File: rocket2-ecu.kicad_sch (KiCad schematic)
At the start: 42 parts, among them J1 ALARM, J12 SMA, J13 ARM Cortex Debug, P1 PAD_SMD, P2 PAD_SMD, P3 PAD_SMD, P4 PAD_SMD, Q1 DMG3402L, U36 AZ1117-3.3

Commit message: Lots of cleanup and updates; Waiting on PR approval for GPS filter
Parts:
- removed C5, C8, C9: 100nF, Capacitor_SMD:C_0603_1608Metric, symbol Device:C_Small
- removed C53, C54, C55: 10uF, Capacitor_SMD:C_0603_1608Metric, symbol Device:C_Small
- removed D35, D36: ESD321, Diode_SMD:D_0402_1005Metric, symbol Device:D_Zener_Small
- removed J13: ARM Cortex Debug, Connector_PinHeader_1.27mm:PinHeader_2x05_P1.27mm_Vertical_SMD, symbol UCIRP-KiCAD-Lib:ARM_Cortex_Debug
- removed J14: ~, Connector_USB:USB_C_Receptacle_GCT_USB4105-xx-A_16P_TopMnt_Horizontal, symbol UCIRP-KiCAD-Lib:USB-C
- removed R3, R4: 4k7, Resistor_SMD:R_0603_1608Metric, symbol Device:R_Small_US
- removed R84, R85: 5.1K, Resistor_SMD:R_0603_1608Metric, symbol Device:R_Small_US
- removed U36: AZ1117-3.3, Package_TO_SOT_SMD:SOT-223-3_TabPin2, symbol Regulator_Linear:AZ1117-3.3
- removed U4: ~, RF_GPS:ublox_SAM-M8Q, symbol UCIRP-KiCAD-Lib:SAM-M8Q
- removed U6: ~, Package_QFP:LQFP-176_24x24mm_P0.5mm, symbol UCIRP-KiCAD-Lib:STM32F469IIT6
- renumbered C6 to C5, C7 to C6, C52 to C7, C51 to C8, J12 to J2, R5 to R3, R6 to R4, U5 to U4, U35 to U5, U34 to U6
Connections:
- no-connect marks 13 -> 0
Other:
- added sheet ECU_STM32 (ecu_stm32.kicad_sch)
- added sheet EVE_GPS (eve_gps.kicad_sch)
- note added: "ETHERNET"
- note added: "STM32 + USB + DEBUG"
- note added: "TRS Radio Module"
- note removed: "*IMPORTANT*"
- note removed: "PCB Considerations (PAGE 12)"
- note removed: "REF (PG 11)"
- company: (none) -> UCI Rocket Project Liquids
- title: (none) -> Rocket2 ECU
- moved on the sheet: C1, C2, C3, C5, C7, C8, J1, J2, P1, P2, P3, P4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

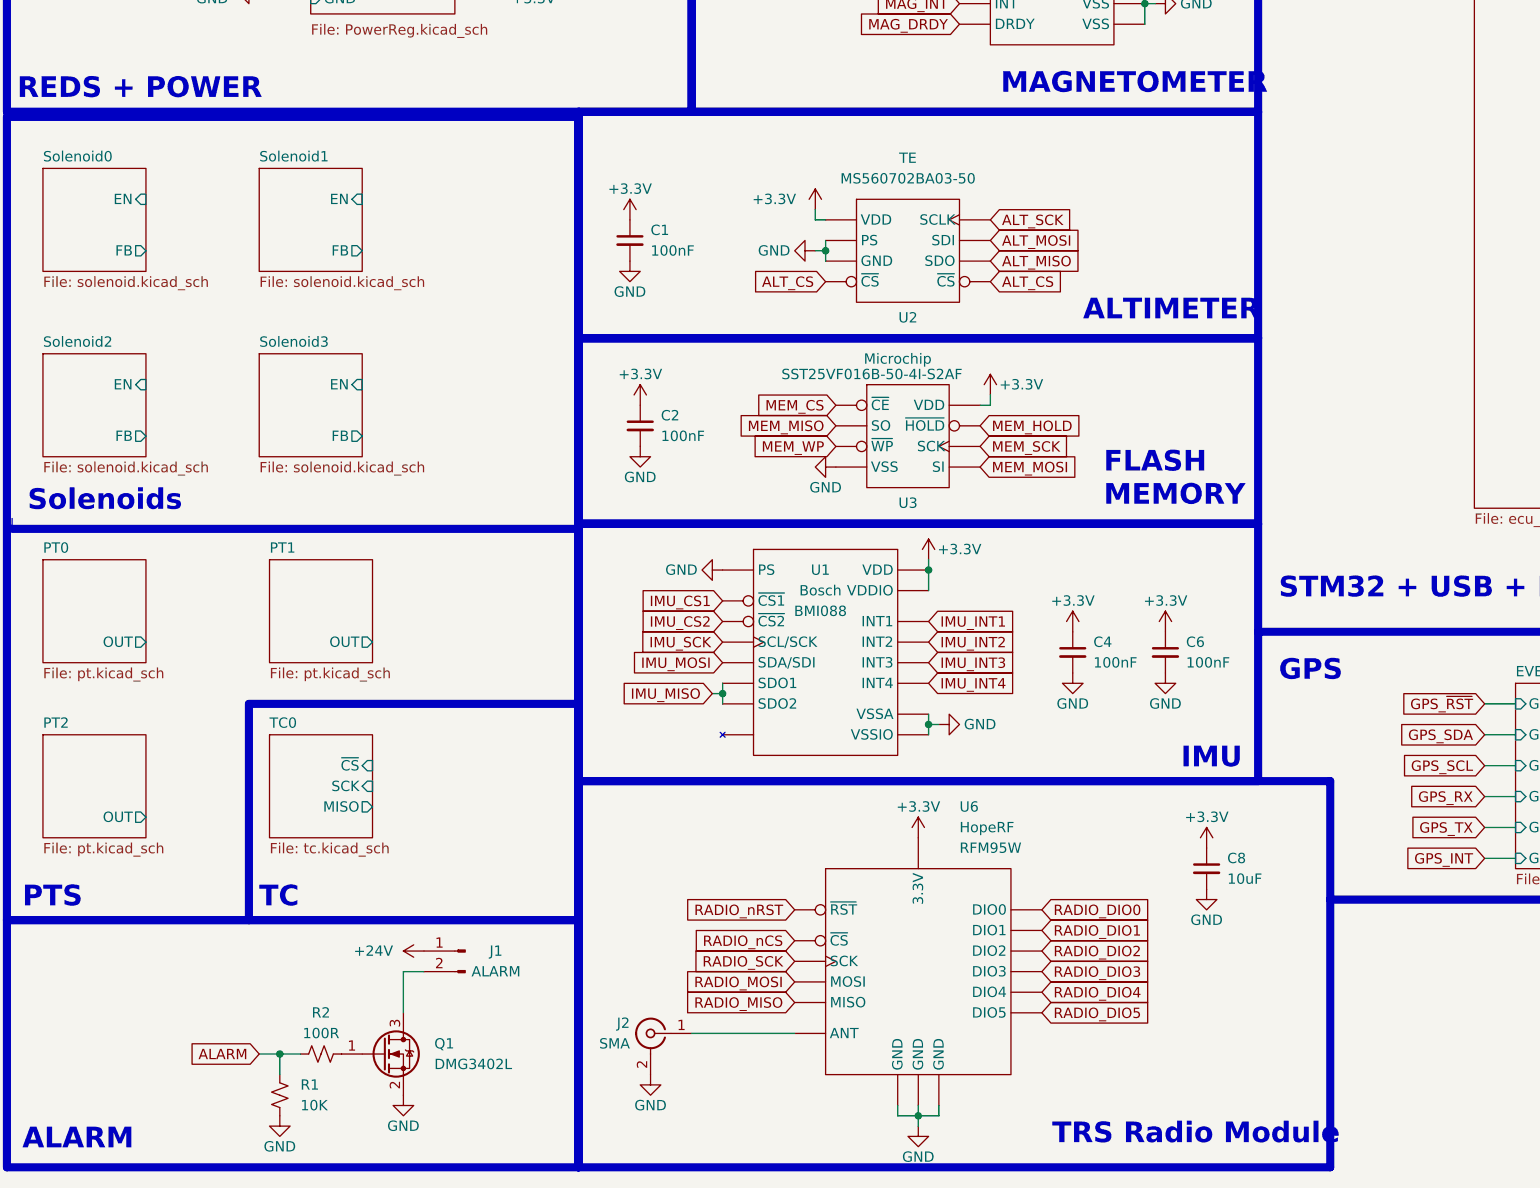
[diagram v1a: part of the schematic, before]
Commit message: changed usb-c, re-named and added some pins
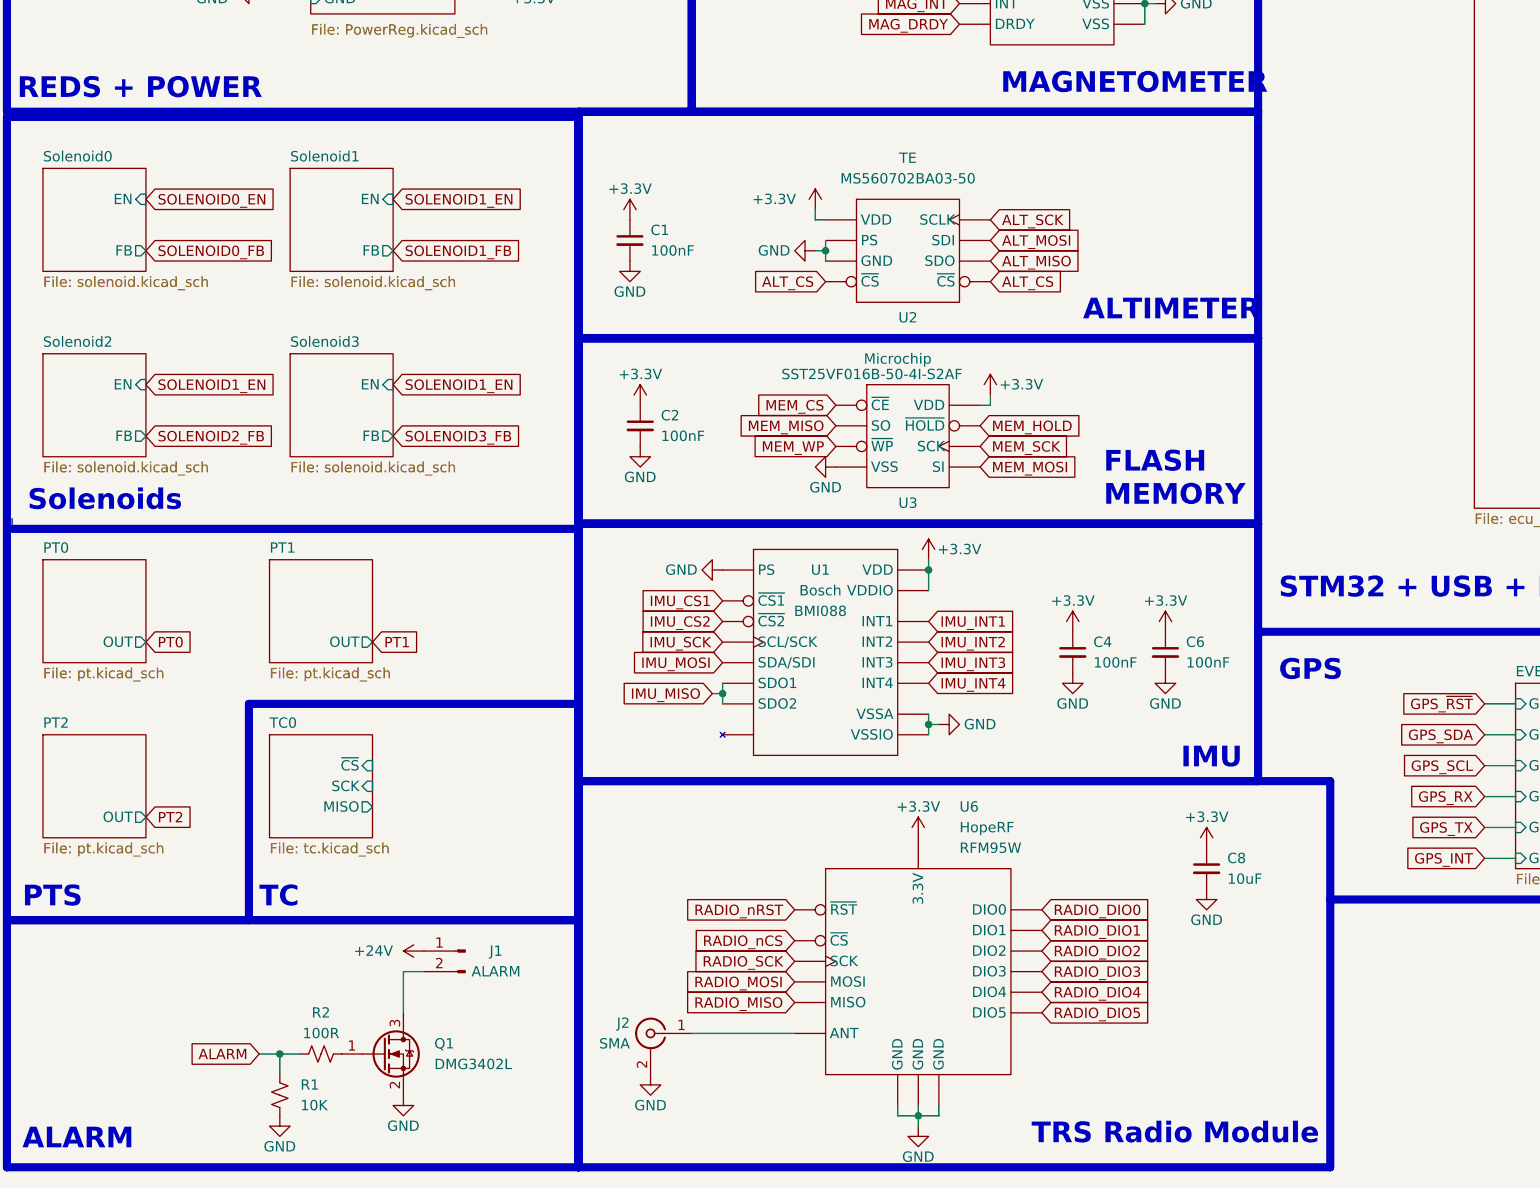
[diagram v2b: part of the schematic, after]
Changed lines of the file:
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@@
     (effects (font (size 2.54 2.54) bold) (justify left bottom))
   )
-  (text "TRS Radio Module" (at 140.97 195.58 0)
+  (text "TRS Radio Module" (at 138.43 195.58 0)
     (effects (font (size 2.54 2.54) bold) (justify left bottom))
   )
@@
     )
   )
+  (global_label "SOLENOID1_EN" (shape input) (at 59.69 101.6 0) (fields_autoplaced)
+    (effects (font (size 1.27 1.27)) (justify left))
+    (property "Intersheetrefs" "${INTERSHEET_REFS}" (at 76.5053 101.6 0)
+      (effects (font (size 1.27 1.27)) (justify left) hide)
+    )
+  )
   (global_label "RADIO_DIO0" (shape input) (at 139.7 166.37 0) (fields_autoplaced)
     (effects (font (size 1.27 1.27)) (justify left))
@@
     )
   )
+  (global_label "PT0" (shape input) (at 29.21 133.35 0) (fields_autoplaced)
+    (effects (font (size 1.27 1.27)) (justify left))
+    (property "Intersheetrefs" "${INTERSHEET_REFS}" (at 35.6423 133.35 0)
+      (effects (font (size 1.27 1.27)) (justify left) hide)
+    )
+  )
+  (global_label "SOLENOID0_FB" (shape input) (at 29.21 85.09 0) (fields_autoplaced)
+    (effects (font (size 1.27 1.27)) (justify left))
+    (property "Intersheetrefs" "${INTERSHEET_REFS}" (at 45.9044 85.09 0)
+      (effects (font (size 1.27 1.27)) (justify left) hide)
+    )
+  )
   (global_label "ALT_CS" (shape input) (at 133.35 88.9 0) (fields_autoplaced)
     (effects (font (size 1.27 1.27)) (justify left))
@@
     )
   )
+  (global_label "SOLENOID3_FB" (shape input) (at 59.69 107.95 0) (fields_autoplaced)
+    (effects (font (size 1.27 1.27)) (justify left))
+    (property "Intersheetrefs" "${INTERSHEET_REFS}" (at 76.3844 107.95 0)
+      (effects (font (size 1.27 1.27)) (justify left) hide)
+    )
+  )
   (global_label "IMU_SCK" (shape input) (at 100.33 133.35 180) (fields_autoplaced)
     (effects (font (size 1.27 1.27)) (justify right))
@@
     (property "Intersheetrefs" "${INTERSHEET_REFS}" (at 95.9538 172.72 0)
       (effects (font (size 1.27 1.27)) (justify right) hide)
+    )
+  )
+  (global_label "SOLENOID1_FB" (shape input) (at 59.69 85.09 0) (fields_autoplaced)
+    (effects (font (size 1.27 1.27)) (justify left))
+    (property "Intersheetrefs" "${INTERSHEET_REFS}" (at 76.3844 85.09 0)
+      (effects (font (size 1.27 1.27)) (justify left) hide)
     )
   )
@@
     )
   )
+  (global_label "SOLENOID1_EN" (shape input) (at 29.21 101.6 0) (fields_autoplaced)
+    (effects (font (size 1.27 1.27)) (justify left))
+    (property "Intersheetrefs" "${INTERSHEET_REFS}" (at 46.0253 101.6 0)
+      (effects (font (size 1.27 1.27)) (justify left) hide)
+    )
+  )
   (global_label "GPS_SCL" (shape input) (at 194.31 148.59 180) (fields_autoplaced)
     (effects (font (size 1.27 1.27)) (justify right))
@@
     (property "Intersheetrefs" "${INTERSHEET_REFS}" (at 230.1506 158.75 0)
       (effects (font (size 1.27 1.27)) (justify right) hide)
+    )
+  )
+  (global_label "SOLENOID1_EN" (shape input) (at 59.69 78.74 0) (fields_autoplaced)
+    (effects (font (size 1.27 1.27)) (justify left))
+    (property "Intersheetrefs" "${INTERSHEET_REFS}" (at 76.5053 78.74 0)
+      (effects (font (size 1.27 1.27)) (justify left) hide)
     )
   )
@@
     )
   )
+  (global_label "PT2" (shape input) (at 29.21 154.94 0) (fields_autoplaced)
+    (effects (font (size 1.27 1.27)) (justify left))
+    (property "Intersheetrefs" "${INTERSHEET_REFS}" (at 35.5629 154.94 0)
+      (effects (font (size 1.27 1.27)) (justify left) hide)
+    )
+  )
+  (global_label "SOLENOID2_FB" (shape input) (at 29.21 107.95 0) (fields_autoplaced)
+    (effects (font (size 1.27 1.27)) (justify left))
+    (property "Intersheetrefs" "${INTERSHEET_REFS}" (at 45.9044 107.95 0)
+      (effects (font (size 1.27 1.27)) (justify left) hide)
+    )
+  )
   (global_label "RADIO_DIO3" (shape input) (at 139.7 173.99 0) (fields_autoplaced)
     (effects (font (size 1.27 1.27)) (justify left))
@@
     )
   )
+  (global_label "PT1" (shape input) (at 57.15 133.35 0) (fields_autoplaced)
+    (effects (font (size 1.27 1.27)) (justify left))
+    (property "Intersheetrefs" "${INTERSHEET_REFS}" (at 63.5029 133.35 0)
+      (effects (font (size 1.27 1.27)) (justify left) hide)
+    )
+  )
   (global_label "RADIO_DIO4" (shape input) (at 139.7 176.53 0) (fields_autoplaced)
     (effects (font (size 1.27 1.27)) (justify left))
@@
     (property "Intersheetrefs" "${INTERSHEET_REFS}" (at 95.1071 177.8 0)
       (effects (font (size 1.27 1.27)) (justify right) hide)
+    )
+  )
+  (global_label "SOLENOID0_EN" (shape input) (at 29.21 78.74 0) (fields_autoplaced)
+    (effects (font (size 1.27 1.27)) (justify left))
+    (property "Intersheetrefs" "${INTERSHEET_REFS}" (at 46.0253 78.74 0)
+      (effects (font (size 1.27 1.27)) (justify left) hide)
     )
   )
@@
     )
   )
-  (sheet (at 43.18 97.79) (size 12.7 12.7) (fields_autoplaced)
+  (sheet (at 46.99 97.79) (size 12.7 12.7) (fields_autoplaced)
     (stroke (width 0.1524) (type solid))
     (fill (color 0 0 0 0.0000))
-    (property "Sheetname" "Solenoid3" (at 43.18 97.0784 0)
+    (property "Sheetname" "Solenoid3" (at 46.99 97.0784 0)
       (effects (font (size 1.27 1.27)) (justify left bottom))
     )
-    (property "Sheetfile" "solenoid.kicad_sch" (at 43.18 111.0746 0)
+    (property "Sheetfile" "solenoid.kicad_sch" (at 46.99 111.0746 0)
       (effects (font (size 1.27 1.27)) (justify left top))
     )
-    (pin "EN" input (at 55.88 101.6 0)
+    (pin "EN" input (at 59.69 101.6 0)
       (effects (font (size 1.27 1.27)) (justify right))
     )
-    (pin "FB" output (at 55.88 107.95 0)
+    (pin "FB" output (at 59.69 107.95 0)
       (effects (font (size 1.27 1.27)) (justify right))
     )
@@
     )
   )
-  (sheet (at 43.18 74.93) (size 12.7 12.7) (fields_autoplaced)
+  (sheet (at 46.99 74.93) (size 12.7 12.7) (fields_autoplaced)
     (stroke (width 0.1524) (type solid))
     (fill (color 0 0 0 0.0000))
-    (property "Sheetname" "Solenoid1" (at 43.18 74.2184 0)
+    (property "Sheetname" "Solenoid1" (at 46.99 74.2184 0)
       (effects (font (size 1.27 1.27)) (justify left bottom))
     )
-    (property "Sheetfile" "solenoid.kicad_sch" (at 43.18 88.2146 0)
+    (property "Sheetfile" "solenoid.kicad_sch" (at 46.99 88.2146 0)
       (effects (font (size 1.27 1.27)) (justify left top))
     )
-    (pin "EN" input (at 55.88 78.74 0)
+    (pin "EN" input (at 59.69 78.74 0)
       (effects (font (size 1.27 1.27)) (justify right))
     )
-    (pin "FB" output (at 55.88 85.09 0)
+    (pin "FB" output (at 59.69 85.09 0)
       (effects (font (size 1.27 1.27)) (justify right))
     )
